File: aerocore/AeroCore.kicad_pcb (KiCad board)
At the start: 2 copper layers, 60 x 60 mm, 55 parts, among them J1 USB_C_Receptacle_USB2.0_16P, J2 Conn_ARM_JTAG_SWD_10, J3 Conn_01x02_Pin, J4 Conn_01x06_Pin, Q1 DMG3418L, U1 RP2040, U2 AP2112K-3.3, U3 MCP73831-2-OT, U4 W25Q16JVUXIQ TR, U5 BMP388, U6 LIS3MDL, U7 ICM-20649, Y2 12MHz

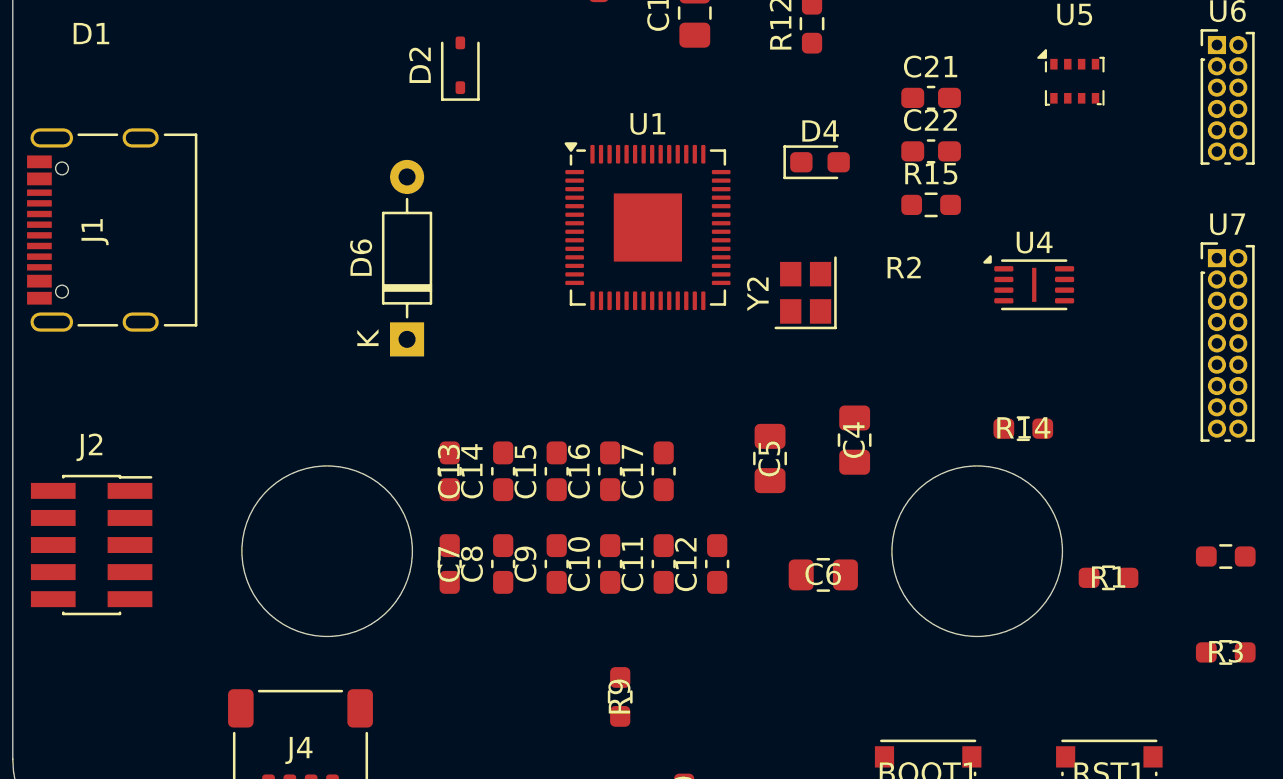
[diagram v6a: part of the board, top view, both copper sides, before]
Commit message: keep rp2040 as mcu
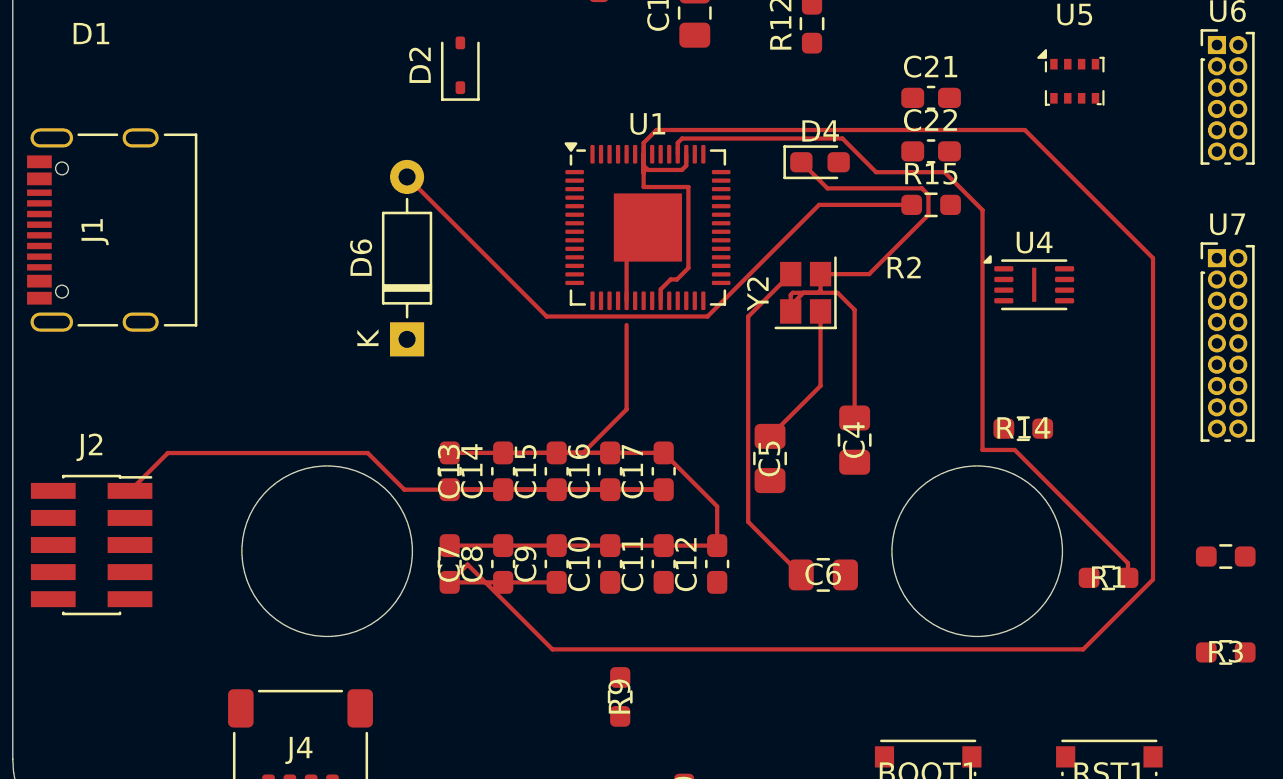
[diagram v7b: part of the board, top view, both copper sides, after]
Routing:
- net /1.2V: track 0.00 -> 97.4 mm
- net GND: track 0.00 -> 70.6 mm
- net /D-: track 0.00 -> 37.3 mm
- net /+3v3: track 0.00 -> 36.5 mm
- net Net-(D6-A): track 0.00 -> 28.6 mm
- net Net-(C6-Pad2): track 0.00 -> 16.0 mm
- net /XIN: track 0.00 -> 6.84 mm

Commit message: add files for final board
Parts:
- added  : LOGO, LOGO, F.Cu at (66.0, 186.2)
- added D7: RED, LED_SMD:LED_0603_1608Metric_Pad1.05x0.95mm_HandSolder, F.Cu at (38.9, 188.0)
- added D8: RED, LED_SMD:LED_0603_1608Metric_Pad1.05x0.95mm_HandSolder, F.Cu at (42.9, 188.0)
- added G***: LOGO, LOGO, F.Cu at (72.8, 134.8)
- added R16: 10k, Resistor_SMD:R_0603_1608Metric_Pad0.98x0.95mm_HandSolder, F.Cu at (38.9, 185.0)
- added R17: 10k, Resistor_SMD:R_0603_1608Metric_Pad0.98x0.95mm_HandSolder, F.Cu at (42.9, 185.0)
- U5: footprint Package_LGA:Bosch_LGA-8_2x2.5mm_P0.65mm_ClockwisePinNumbering -> easyeda2kicad:SENSORM-SMD_BMP388
- U6: footprint Connector_PinHeader_1.00mm:PinHeader_2x06_P1.00mm_Vertical -> easyeda2kicad:LGA-12_L2.0-W2.0-P0.50-BL
- U7: footprint Connector_PinHeader_1.00mm:PinHeader_2x09_P1.00mm_Vertical -> easyeda2kicad:QFN-24_L3.0-W3.0-P0.40-TL-EP1.4
- moved R8 62.5 mm to (31.1, 185.0), turned to 0 degrees
- moved RST1 60.7 mm to (23.5, 148.5), turned to 90 degrees
- moved J2 60.5 mm to (74.7, 142.5)
- moved J4 52.1 mm to (74.2, 152.0), turned to 90 degrees
- moved R3 47.8 mm to (32.2, 163.0), turned to 180 degrees
- moved R7 47.2 mm to (41.8, 164.2), turned to 90 degrees
- moved R2 47.0 mm to (32.2, 161.0)
- moved D3 44.9 mm to (35.0, 188.0)
- moved R1 43.9 mm to (32.2, 156.8)
- moved BOOT1 42.1 mm to (23.5, 171.0), turned to 90 degrees
- moved D4 40.9 mm to (31.1, 188.0)
- moved R4 40.8 mm to (32.2, 155.0), turned to 0 degrees
- moved C4 36.1 mm to (58.5, 134.0), turned to 180 degrees
- moved R5 32.9 mm to (26.0, 135.5), turned to -90 degrees
- moved R14 31.7 mm to (38.6, 156.2)
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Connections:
- R10 pad 1: /D13 -> /D15
- R8 pad 1: /D14 -> /D16
- U1 pad 28: /D17 -> /CS_3
- U1 pad 3: /D1 -> /CS_2
- U1 pad 4: /D2 -> /SCK0
- U1 pad 5: /D3 -> /MOSI0
- U1 pad 6: /D4 -> /MISO0
- U1 pad 7: /D5 -> /CS_1
- U1 pad 8: /D6 -> /SDA
- U1 pad 9: /D7 -> /SCL
- U5 pad 2: /SCK -> /SCK0
- U5 pad 4: /MOSI -> /MOSI0
- U5 pad 5: /MISO -> /MISO0
- U6 pad 1: /SCK -> /SCK0
- U6 pad 11: /MOSI -> /MOSI0
- U6 pad 9: /MISO -> /MISO0
- U7 pad 9: /MISO -> /MISO0
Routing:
- net /+3v3: track 36.5 -> 325.3 mm, vias 0 -> 9
- net GND: track 70.6 -> 349.7 mm, vias 0 -> 6
- net /~{RESET}: track 0.00 -> 91.4 mm, vias 0 -> 5
- net /VBUS: track 0.00 -> 77.0 mm, vias 0 -> 2
- net /1.2V: track 97.4 -> 21.2 mm
- net /MISO0: track 0.00 -> 76.1 mm, vias 0 -> 5
- net /MOSI0: track 0.00 -> 75.7 mm, vias 0 -> 4
- net /SCK0: track 0.00 -> 74.6 mm, vias 0 -> 4
- net /SDA: track 0.00 -> 53.8 mm, vias 0 -> 2
- net /SWDIO: track 0.00 -> 50.4 mm, vias 0 -> 2
- net /SWCLK: track 0.00 -> 47.8 mm, vias 0 -> 2
- net /SCL: track 0.00 -> 44.8 mm, vias 0 -> 2
- net /D16: track 0.00 -> 40.8 mm, vias 0 -> 2
- net /QSPI_CS: track 0.00 -> 39.3 mm, vias 0 -> 2
- net /CS_3: track 0.00 -> 38.9 mm, vias 0 -> 2
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- added copper zone on B.Cu, net GND
- added copper zone on F.Cu, net GND
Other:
- board text added: "Aeronode"
- board text added: "v0.0.1"
- board text removed: "AeroNode"
